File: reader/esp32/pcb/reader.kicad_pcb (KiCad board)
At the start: 2 copper layers, 96.5 x 30.1 mm, 28 parts, among them J1 Conn_01x06, J2 Conn_01x02, J3 Conn_01x04, J4 Conn_01x02, Q1 MMBT3904, Q2 MMBT3904, U1 ESP32-WROOM-32U, U2 RF125-PS, U3 CH340C, U4 74LVC1T45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

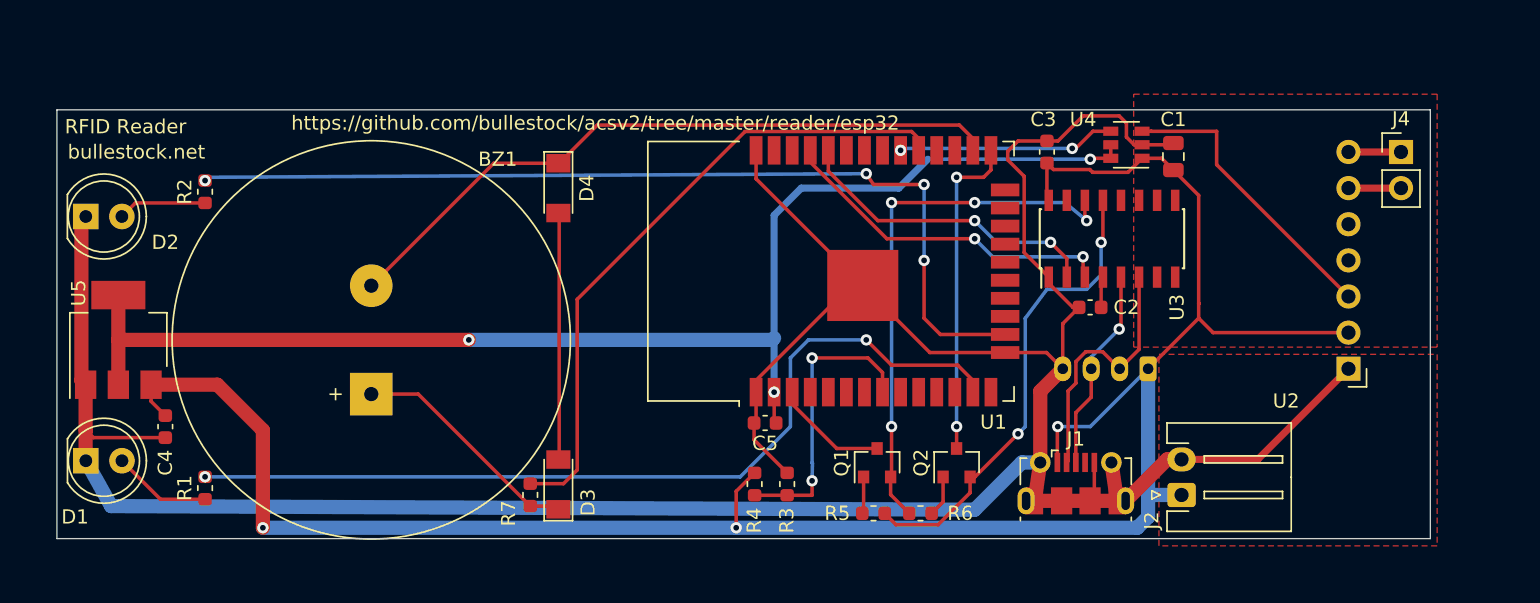
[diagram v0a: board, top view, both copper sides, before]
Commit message: Fix silkscreen issue; adapt buzzer footprint for 10 mm pin spacing.
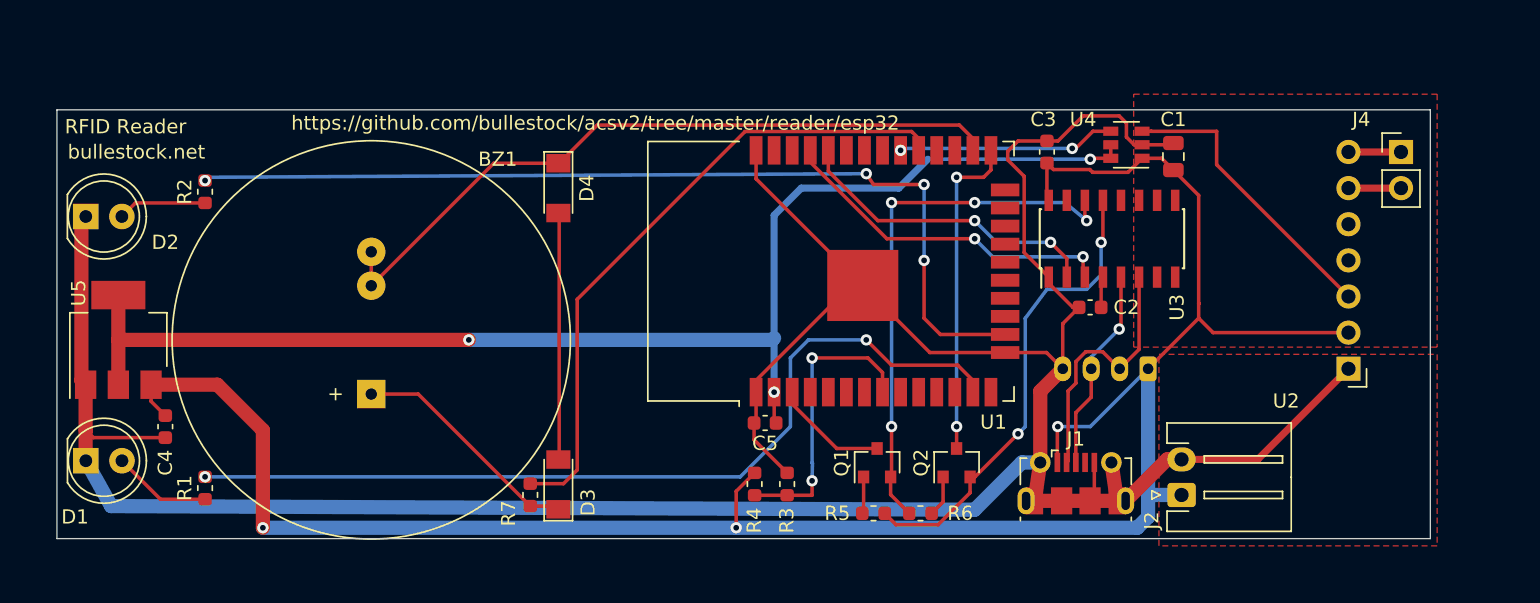
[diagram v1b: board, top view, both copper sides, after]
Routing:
- net BUZ2: track 47.4 -> 49.7 mm
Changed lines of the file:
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@@
-(kicad_pcb (version 20210606) (generator pcbnew)
+(kicad_pcb (version 20211014) (generator pcbnew)
   (general
     (thickness 1.6)
@@
     )
     (fp_line (start -1.29 -1.545) (end -1.29 1.545) (layer "F.SilkS") (width 0.12))
-    (fp_arc (start 1.27 0) (end -1.29 1.54483) (angle -148.9) (layer "F.SilkS") (width 0.12))
-    (fp_arc (start 1.27 0) (end -1.29 -1.54483) (angle 148.9) (layer "F.SilkS") (width 0.12))
+    (fp_arc (start 4.26 -0.000462) (mid 2.072002 2.880433) (end -1.29 1.54483) (layer "F.SilkS") (width 0.12))
+    (fp_arc (start -1.29 -1.54483) (mid 2.072002 -2.880433) (end 4.26 0.000462) (layer "F.SilkS") (width 0.12))
     (fp_circle (center 1.27 0) (end 3.77 0) (layer "F.SilkS") (width 0.12) (fill none))
     (fp_line (start -1.95 -3.25) (end -1.95 3.25) (layer "F.CrtYd") (width 0.05))
@@
     (fp_line (start -1.95 3.25) (end 4.5 3.25) (layer "F.CrtYd") (width 0.05))
     (fp_line (start -1.23 -1.469694) (end -1.23 1.469694) (layer "F.Fab") (width 0.1))
-    (fp_arc (start 1.27 0) (end -1.23 -1.469694) (angle 299.1) (layer "F.Fab") (width 0.1))
+    (fp_arc (start -1.23 -1.469694) (mid 4.17 0.000016) (end -1.230016 1.469666) (layer "F.Fab") (width 0.1))
     (fp_circle (center 1.27 0) (end 3.77 0) (layer "F.Fab") (width 0.1) (fill none))
     (pad "1" thru_hole rect locked (at 0 0) (size 1.8 1.8) (drill 0.9) (layers *.Cu *.Mask) (remove_unused_layers) (keep_end_layers)
@@
     (fp_circle (center 5 0) (end 6 0) (layer "F.Fab") (width 0.1) (fill none))
     (fp_circle (center 3.81 0) (end 14.91 0) (layer "F.Fab") (width 0.1) (fill none))
-    (pad "1" thru_hole rect locked (at 0 0 90) (size 3 3) (drill 1) (layers *.Cu *.Mask) (remove_unused_layers) (keep_end_layers)
+    (pad "1" thru_hole rect (at 0 0 90) (size 2 2) (drill 0.8) (layers *.Cu *.Mask) (remove_unused_layers) (keep_end_layers)
       (net 9 "Net-(BZ1-Pad1)") (pinfunction "-") (pintype "passive"))
-    (pad "2" thru_hole circle locked (at 7.62 0 90) (size 3 3) (drill 1) (layers *.Cu *.Mask) (remove_unused_layers) (keep_end_layers)
+    (pad "2" thru_hole circle (at 10 0 90) (size 2 2) (drill 0.8) (layers *.Cu *.Mask)
+      (net 1 "BUZ2") (pinfunction "+") (pintype "passive"))
+    (pad "2" thru_hole circle (at 7.62 0 90) (size 2 2) (drill 0.8) (layers *.Cu *.Mask) (remove_unused_layers) (keep_end_layers)
       (net 1 "BUZ2") (pinfunction "+") (pintype "passive"))
     (model "${KISYS3DMOD}/Buzzer_Beeper.3dshapes/Buzzer_D14mm_H7mm_P10mm.wrl"
@@
     )
     (fp_line (start -1.29 -1.545) (end -1.29 1.545) (layer "F.SilkS") (width 0.12))
-    (fp_arc (start 1.27 0) (end -1.29 -1.54483) (angle 148.9) (layer "F.SilkS") (width 0.12))
-    (fp_arc (start 1.27 0) (end -1.29 1.54483) (angle -148.9) (layer "F.SilkS") (width 0.12))
+    (fp_arc (start -1.29 -1.54483) (mid 2.072002 -2.880433) (end 4.26 0.000462) (layer "F.SilkS") (width 0.12))
+    (fp_arc (start 4.26 -0.000462) (mid 2.072002 2.880433) (end -1.29 1.54483) (layer "F.SilkS") (width 0.12))
     (fp_circle (center 1.27 0) (end 3.77 0) (layer "F.SilkS") (width 0.12) (fill none))
     (fp_line (start 4.5 -3.25) (end -1.95 -3.25) (layer "F.CrtYd") (width 0.05))
@@
     (fp_line (start -1.95 3.25) (end 4.5 3.25) (layer "F.CrtYd") (width 0.05))
     (fp_line (start -1.23 -1.469694) (end -1.23 1.469694) (layer "F.Fab") (width 0.1))
-    (fp_arc (start 1.27 0) (end -1.23 -1.469694) (angle 299.1) (layer "F.Fab") (width 0.1))
+    (fp_arc (start -1.23 -1.469694) (mid 4.17 0.000016) (end -1.230016 1.469666) (layer "F.Fab") (width 0.1))
     (fp_circle (center 1.27 0) (end 3.77 0) (layer "F.Fab") (width 0.1) (fill none))
     (pad "1" thru_hole rect locked (at 0 0) (size 1.8 1.8) (drill 0.9) (layers *.Cu *.Mask) (remove_unused_layers) (keep_end_layers)
@@
     (property "Sheetname" "")
     (attr through_hole)
-    (fp_text reference "J4" (at 0 -2.33) (layer "F.SilkS")
+    (fp_text reference "J4" (at -2.794 -2.286) (layer "F.SilkS")
       (effects (font (size 1 1) (thickness 0.15)))
     )
@@
   (segment (start 79.756 46.256) (end 75.156 46.256) (width 0.25) (layer "F.Cu") (net 1))
   (segment (start 75.156 46.256) (end 66.548 54.864) (width 0.25) (layer "F.Cu") (net 1))
+  (segment (start 66.548 52.484) (end 66.548 54.864) (width 0.25) (layer "F.Cu") (net 1))
   (segment (start 79.756 46.256) (end 82.438022 43.573978) (width 0.25) (layer "F.Cu") (net 1))
   (segment (start 81.026 67.818) (end 80.061 68.783) (width 0.25) (layer "F.Cu") (net 2))

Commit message: Fix 3D models.
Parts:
- J4: footprint Connector_PinHeader_2.54mm:PinHeader_1x02_P2.54mm_Vertical -> Connector_JST:JST_XH_S02B-XH-A-1_1x02_P2.50mm_Horizontal
- moved J4 2.52 mm to (138.9, 48.0), turned to 90 degrees
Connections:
- J1 pad 3: Net-(J3-Pad3) -> Net-(J1-Pad3)
- J3 pad 3: Net-(J3-Pad3) -> Net-(J1-Pad3)
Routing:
- net Net-(J3-Pad3): track 14.3 -> 0.00 mm, vias 1 -> 0
- net Net-(J1-Pad3): track 0.00 -> 14.3 mm, vias 0 -> 1

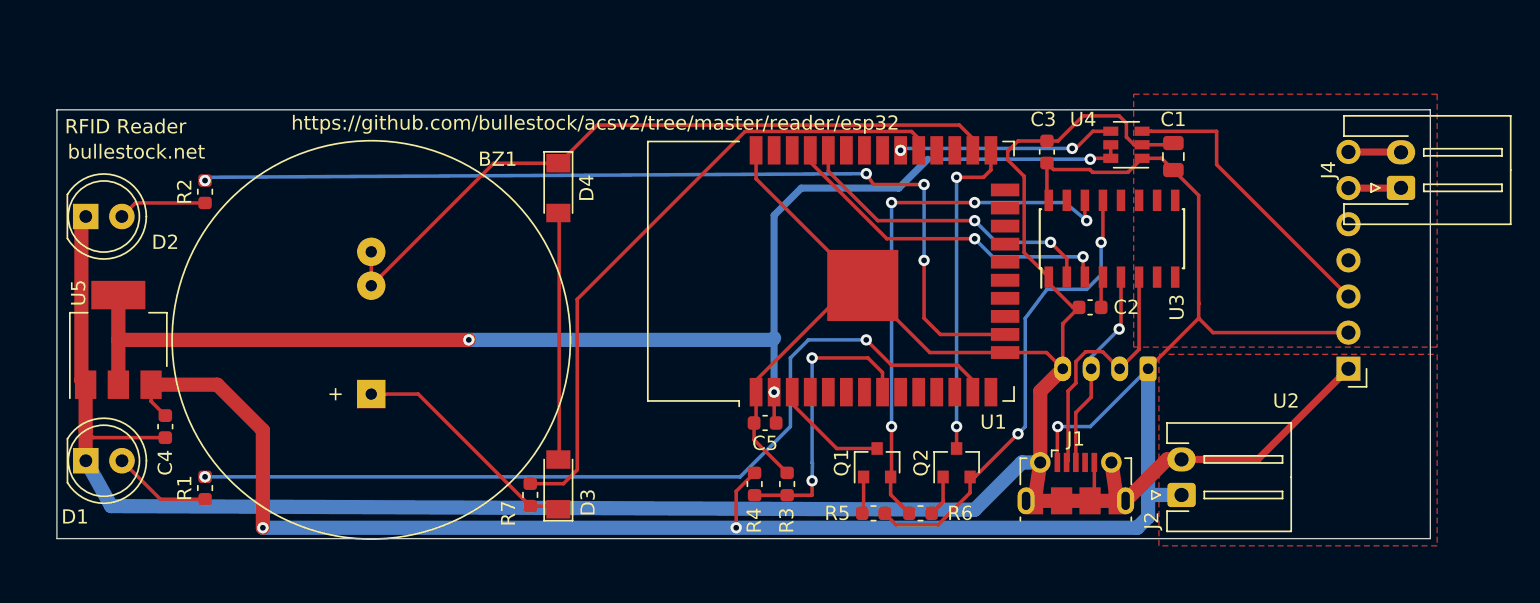
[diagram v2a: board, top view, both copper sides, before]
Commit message: Retry reopen of serial port.
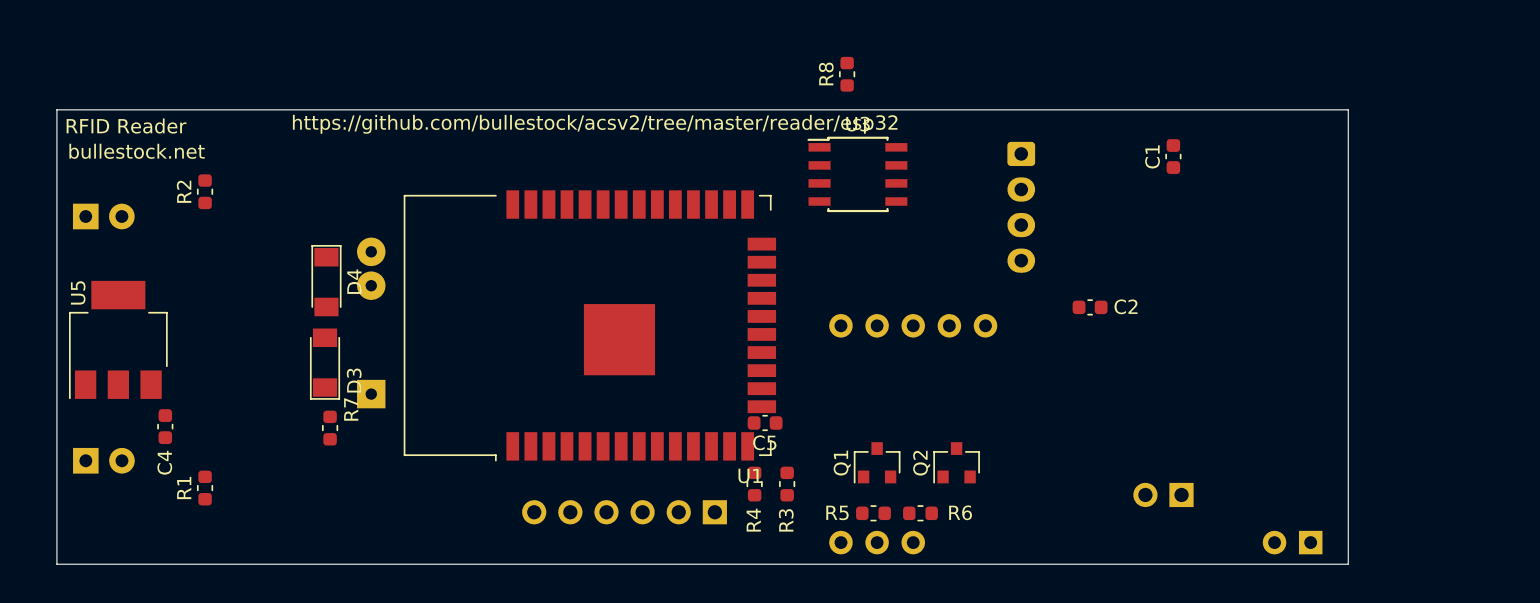
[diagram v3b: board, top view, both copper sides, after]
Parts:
- removed C3: C, Capacitor_SMD:C_0603_1608Metric
- removed J4: Conn_01x02, Connector_JST:JST_XH_S02B-XH-A-1_1x02_P2.50mm_Horizontal
- removed U4: 74LVC1T45, Package_TO_SOT_SMD:SOT-23-6
- added R8: 120, Resistor_SMD:R_0603_1608Metric, F.Cu at (100.0, 40.0)
- BZ1, D1, D2: moved to B.Cu
- C1: footprint Capacitor_SMD:C_0805_2012Metric -> Capacitor_SMD:C_0603_1608Metric
- C2: value C -> 100n
- J1: value Conn_01x06 -> Debug; footprint Connector_USB:USB_Micro-B_Molex-105017-0001 -> Connector_PinHeader_2.54mm:PinHeader_1x06_P2.54mm_Vertical; moved to B.Cu
- J2: value Conn_01x02 -> RFID; footprint Connector_JST:JST_XH_S02B-XH-A-1_1x02_P2.50mm_Horizontal -> Connector_PinHeader_2.54mm:PinHeader_1x02_P2.54mm_Vertical; moved to B.Cu
- J3: footprint Connector_JST:JST_PH_B4B-PH-K_1x04_P2.00mm_Vertical -> Connector_JST:JST_XH_S04B-XH-A_1x04_P2.50mm_Horizontal
- R3, R5: value 10K -> 1k2
- R4, R6: value 10K -> 2k2
- U2: value RF125-PS -> RDM6300; footprint Module:rf125ps -> Module:RDM6300_B38.5x18.2mm; moved to B.Cu
- U3: value CH340C -> MAX485E; footprint Housings_SOIC:SOIC-16_3.9x9.9mm_Pitch1.27mm -> Housings_SOIC:SOIC-8_3.9x4.9mm_Pitch1.27mm
- moved J1 25.5 mm to (90.7, 70.8), turned to 90 degrees
- moved D3 18.5 mm to (63.3, 60.3)
- moved U3 18.4 mm to (100.8, 47.0), turned to 0 degrees
- moved D4 17.6 mm to (63.4, 54.6)
- moved J3 17.5 mm to (112.2, 45.6), turned to -90 degrees
- moved U1 17.5 mm to (84.8, 57.7)
- moved R7 14.8 mm to (63.7, 64.9), turned to 90 degrees
- moved U2 12.5 mm to (132.6, 72.9)
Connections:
- C2 pad 1: Net-(C2-Pad1) -> +5V
- J1 pad 1: +5V -> GND
- J1 pad 2: Net-(J1-Pad2) -> RTS
- J1 pad 3: Net-(J1-Pad3) -> +5V
- J1 pad 4: unconnected-(J1-Pad4) -> Net-(J1-Pin_4)
- J1 pad 5: GND -> ESP_TX
- J1 pad 6: GND -> DTR
- J2 pad 1: +5V -> Net-(J2-Pin_1)
- J2 pad 2: GND -> Net-(J2-Pin_2)
- J3 pad 1: +5V -> GND
- J3 pad 2: Net-(J1-Pad2) -> Net-(J3-Pin_2)
- J3 pad 3: Net-(J1-Pad3) -> Net-(J3-Pin_3)
- J3 pad 4: GND -> +5V
- Q1 pad 1: Net-(Q1-Pad1) -> RTS
- Q1 pad 2: Net-(Q1-Pad2) -> DTR
- Q1 pad 3: EN -> BOOT
- Q2 pad 1: Net-(Q2-Pad1) -> DTR
- Q2 pad 2: Net-(Q2-Pad2) -> RTS
- Q2 pad 3: IO0 -> RESET
- R3 pad 1: +5V -> Net-(J1-Pin_4)
- R3 pad 2: SENSE -> ESP_RX
- R4 pad 1: SENSE -> ESP_RX
- R5 pad 1: Net-(Q2-Pad2) -> Net-(U2-TX)
- R5 pad 2: Net-(Q1-Pad1) -> ESP_RFID_TX
- R6 pad 1: Net-(Q1-Pad2) -> ESP_RFID_TX
- R6 pad 2: Net-(Q2-Pad1) -> GND
- U1 pad 25: IO0 -> BOOT
- U1 pad 3: EN -> RESET
- U1 pad 33: unconnected-(U1-Pad33) -> RTS
- U1 pad 36: unconnected-(U1-Pad36) -> RX485
- U1 pad 37: unconnected-(U1-Pad37) -> TX485
- U1 pad 8: SENSE -> unconnected-(U1-IO32-Pad8)
- U2 pad 1: GND -> Net-(J2-Pin_1)
- U2 pad 2: +5V -> Net-(J2-Pin_2)
- U2 pad 3: Net-(U2-Pad3) -> GND
- U2 pad 4: unconnected-(U2-Pad4) -> +5V
- U2 pad 6: Net-(J4-Pad2) -> Net-(U2-TX)
- U2 pad 7: Net-(J4-Pad1) -> unconnected-(U2-RX-Pad7)
- U3 pad 1: GND -> RX485
- U3 pad 2: ESP_RX -> RTS
- U3 pad 3: ESP_TX -> RTS
- U3 pad 4: Net-(C2-Pad1) -> TX485
- U3 pad 5: Net-(J3-Pad3) -> GND
- U3 pad 6: Net-(J1-Pad2) -> Net-(J3-Pin_2)
- U3 pad 7: (no net) -> Net-(J3-Pin_3)
- U3 pad 8: (no net) -> +5V
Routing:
- net GND: track 211.4 -> 0.00 mm
- net +5V: track 148.5 -> 0.00 mm, vias 3 -> 0
- net +3V3: track 93.2 -> 0.00 mm, vias 3 -> 0
- net GREEN: track 66.6 -> 0.00 mm, vias 4 -> 0
- net RED: track 62.0 -> 0.00 mm, vias 2 -> 0
- net BUZ2: track 49.7 -> 0.00 mm
- net BUZ1: track 44.8 -> 0.00 mm
- net Net-(Q1-Pad2): track 38.0 -> 0.00 mm, vias 4 -> 0
- net Net-(Q2-Pad2): track 33.4 -> 0.00 mm, vias 2 -> 0
- net ESP_TX: track 23.2 -> 0.00 mm, vias 2 -> 0
- net IO0: track 23.1 -> 0.00 mm, vias 2 -> 0
- net ESP_RX: track 22.1 -> 0.00 mm, vias 2 -> 0
- net Net-(U2-Pad3): track 20.7 -> 0.00 mm
- net SENSE: track 20.5 -> 0.00 mm, vias 2 -> 0
- net Net-(J1-Pad2): track 18.2 -> 0.00 mm
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- removed copper zone on F.Cu, net +5V
- removed copper zone on F.Cu, net GND
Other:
- board size 96.5 x 30.1 mm -> 90.8 x 31.9 mm

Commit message: USe RS-485 instead of USB.
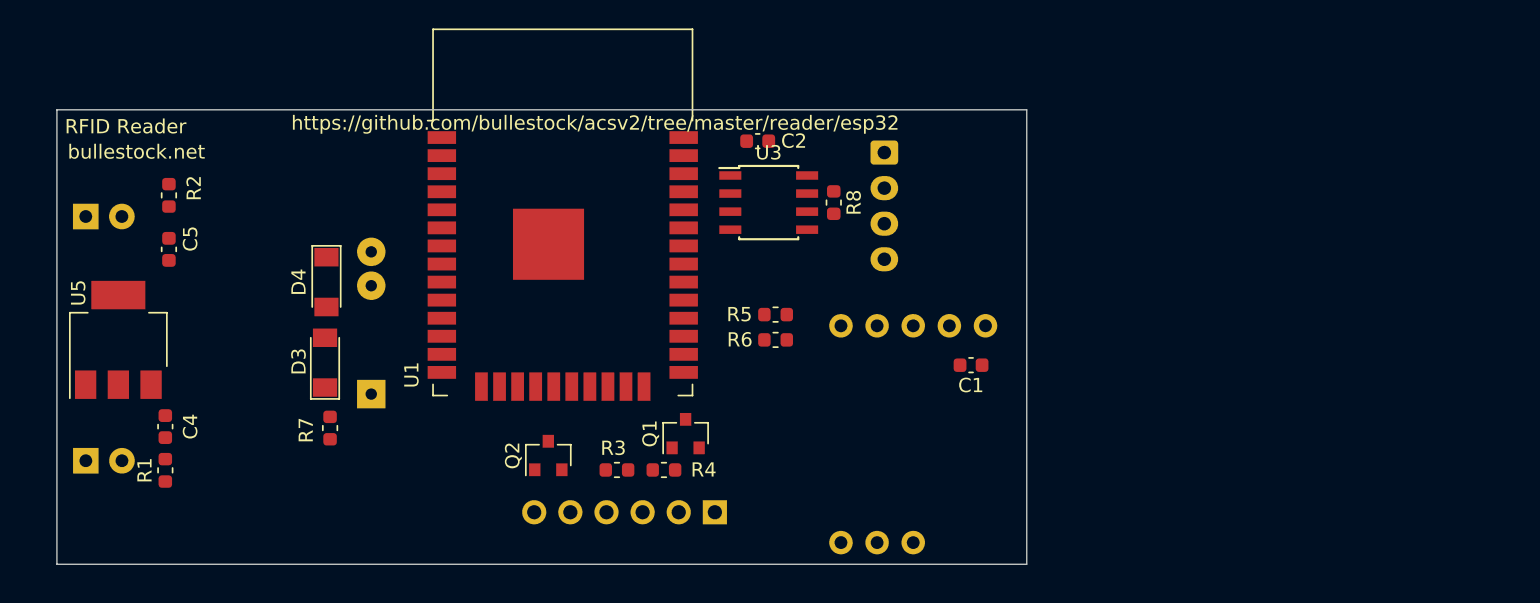
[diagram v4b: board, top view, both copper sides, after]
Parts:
- removed J3: Conn_01x04, Connector_JST:JST_XH_S04B-XH-A_1x04_P2.50mm_Horizontal
- J2: value RFID -> RS485; footprint Connector_PinHeader_2.54mm:PinHeader_1x02_P2.54mm_Vertical -> Connector_JST:JST_XH_S04B-XH-A_1x04_P2.50mm_Horizontal
- moved C5 43.7 mm to (52.3, 52.3), turned to 90 degrees
- moved J2 31.9 mm to (102.6, 45.5), turned to -90 degrees
- moved Q2 28.7 mm to (79.0, 66.8)
- moved C2 26.1 mm to (93.7, 44.7)
- moved C1 20.4 mm to (108.7, 60.5), turned to 180 degrees
- moved R6 15.9 mm to (95.0, 58.7)
- moved R5 15.6 mm to (95.0, 56.9)
- moved Q1 13.6 mm to (88.6, 65.3)
- moved R3 9.73 mm to (83.8, 67.8), turned to 0 degrees
- moved R8 9.07 mm to (99.1, 49.0), turned to -90 degrees
- moved R4 8.72 mm to (87.1, 67.8), turned to 0 degrees
- moved U1 6.86 mm to (80.0, 52.7), turned to 0 degrees
- moved U3 6.58 mm to (94.5, 49.0)
- moved R1 3.06 mm to (52.1, 67.8)
- moved R2 2.55 mm to (52.3, 48.5)
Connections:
- J2 pad 1: Net-(J2-Pin_1) -> +5V
- R8 pad 1: Net-(J3-Pin_3) -> Net-(J2-Pin_2)
- R8 pad 2: Net-(J3-Pin_2) -> Net-(J2-Pin_3)
- U1 pad 10: unconnected-(U1-IO25-Pad10) -> GREEN
- U1 pad 11: unconnected-(U1-IO26-Pad11) -> BUZ2
- U1 pad 12: unconnected-(U1-IO27-Pad12) -> BUZ1
- U1 pad 16: GREEN -> unconnected-(U1-IO13-Pad16)
- U1 pad 26: BUZ2 -> unconnected-(U1-IO4-Pad26)
- U1 pad 29: BUZ1 -> unconnected-(U1-IO5-Pad29)
- U3 pad 6: Net-(J3-Pin_2) -> Net-(J2-Pin_3)
- U3 pad 7: Net-(J3-Pin_3) -> Net-(J2-Pin_2)
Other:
- board size 90.8 x 31.9 mm -> 68.2 x 31.9 mm
